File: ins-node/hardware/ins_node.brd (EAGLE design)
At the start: 54.7 x 43.2 mm, 11 parts, among them Q3 MOSFET-2N7000, U1 TINY85-20-DIP

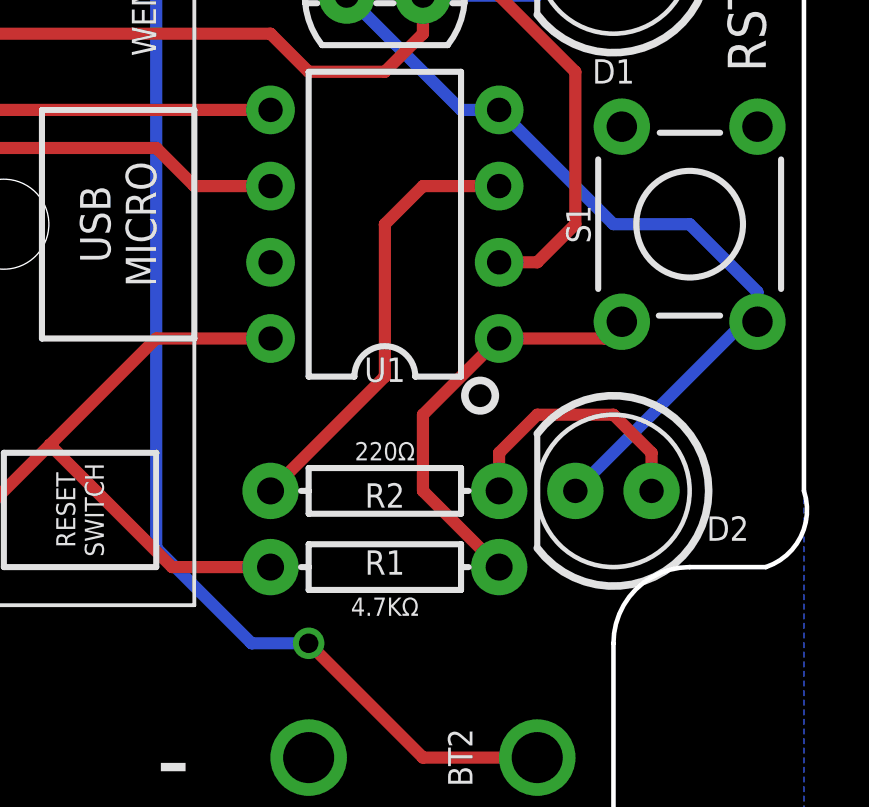
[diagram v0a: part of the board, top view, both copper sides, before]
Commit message: Add decoupling capacitor
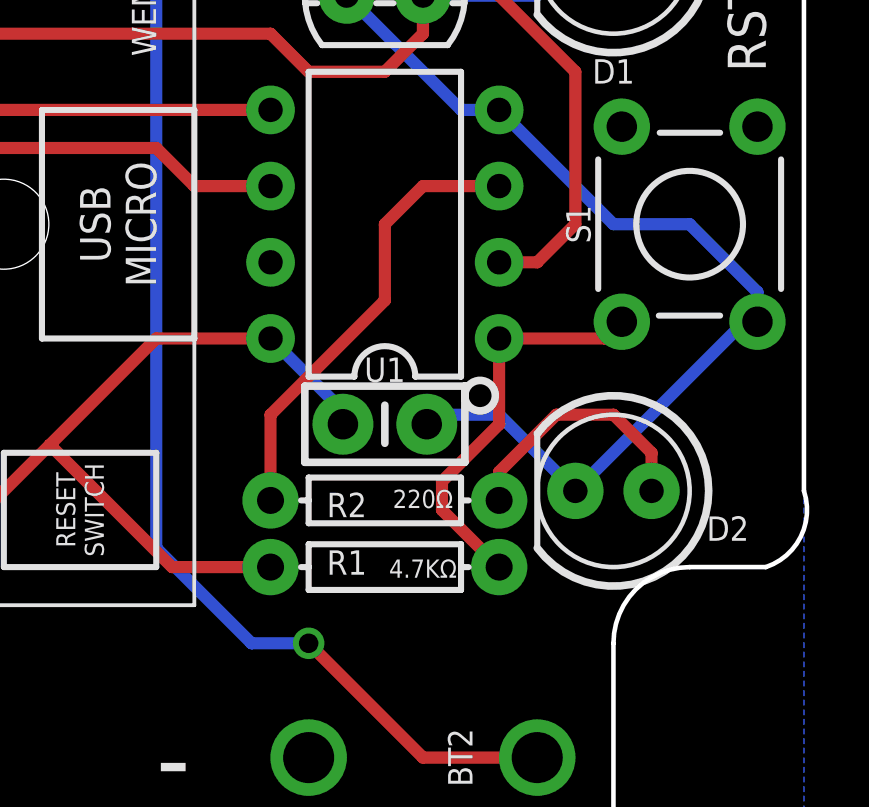
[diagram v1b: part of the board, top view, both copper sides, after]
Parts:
- added C1: 0.1uF, SparkFun-Capacitors:CAP-PTH-SMALL-KIT
- moved R2 0.32 mm to (66.0, 42.9)
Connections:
- net GND: now also C1.2
- net VCC: now also C1.1
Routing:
- net GND: track 80.6 -> 86.7 mm
- net VCC: track 52.7 -> 56.6 mm
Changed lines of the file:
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@@
 </element>
 <element name="R1" library="SparkFun-Resistors" library_urn="urn:adsk.eagle:library:532" package="AXIAL-0.3" package3d_urn="urn:adsk.eagle:package:39658/1" value="4.7KΩ" x="66.04" y="40.64" smashed="yes">
-<attribute name="NAME" x="66.04" y="40.386" size="0.8128" layer="25" font="vector" ratio="20" align="bottom-center"/>
+<attribute name="NAME" x="64.77" y="40.386" size="0.8128" layer="25" font="vector" ratio="20" align="bottom-center"/>
 <attribute name="PROD_ID" value=" " x="66.04" y="40.64" size="1.778" layer="27" display="off"/>
-<attribute name="VALUE" x="66.04" y="39.624" size="0.6096" layer="25" font="vector" ratio="20" align="top-center"/>
+<attribute name="VALUE" x="67.31" y="40.894" size="0.6096" layer="25" font="vector" ratio="20" align="top-center"/>
 </element>
-<element name="R2" library="SparkFun-Resistors" library_urn="urn:adsk.eagle:library:532" package="AXIAL-0.3" package3d_urn="urn:adsk.eagle:package:39658/1" value="220Ω" x="66.04" y="43.18" smashed="yes" rot="R180">
-<attribute name="NAME" x="66.04" y="43.434" size="0.8128" layer="25" font="vector" ratio="20" rot="R180" align="bottom-center"/>
-<attribute name="PROD_ID" value=" " x="66.04" y="43.18" size="1.778" layer="27" rot="R180" display="off"/>
-<attribute name="VALUE" x="66.04" y="44.196" size="0.6096" layer="25" font="vector" ratio="20" rot="R180" align="top-center"/>
+<element name="R2" library="SparkFun-Resistors" library_urn="urn:adsk.eagle:library:532" package="AXIAL-0.3" package3d_urn="urn:adsk.eagle:package:39658/1" value="220Ω" x="66.04" y="42.8625" smashed="yes" rot="R180">
+<attribute name="NAME" x="64.77" y="43.1165" size="0.8128" layer="25" font="vector" ratio="20" rot="R180" align="bottom-center"/>
+<attribute name="PROD_ID" value=" " x="66.04" y="42.8625" size="1.778" layer="27" rot="R180" display="off"/>
+<attribute name="VALUE" x="67.31" y="42.6085" size="0.6096" layer="25" font="vector" ratio="20" rot="R180" align="top-center"/>
 </element>
 <element name="R3" library="SparkFun-Resistors" library_urn="urn:adsk.eagle:library:532" package="AXIAL-0.3" package3d_urn="urn:adsk.eagle:package:39658/1" value="220Ω" x="66.04" y="63.5" smashed="yes" rot="R180">
@@
 <attribute name="NAME" x="77.47" y="42.3291" size="0.8128" layer="25" font="vector" ratio="20" rot="R180" align="bottom-center"/>
 <attribute name="VALUE" x="73.6346" y="46.5709" size="0.6096" layer="27" font="vector" ratio="20" rot="R180" align="top-center"/>
+</element>
+<element name="C1" library="SparkFun-Capacitors" library_urn="urn:adsk.eagle:library:510" package="CAP-PTH-SMALL-KIT" package3d_urn="urn:adsk.eagle:package:37428/1" value="0.1uF" x="66.04" y="45.4025" smashed="yes">
+<attribute name="PROD_ID" value="CAP-08370" x="66.04" y="45.4025" size="1.27" layer="27" ratio="15" display="off"/>
 </element>
 </elements>
@@
 <vertex x="25.4" y="30.48"/>
 </polygon>
+<contactref element="C1" pad="2"/>
+<wire x1="72.39" y1="43.18" x2="69.85" y2="45.72" width="0.4064" layer="16"/>
+<wire x1="69.85" y1="45.72" x2="67.7545" y2="45.72" width="0.4064" layer="16"/>
+<wire x1="67.7545" y1="45.72" x2="67.437" y2="45.4025" width="0.4064" layer="16"/>
 </signal>
 <signal name="VCC">
@@
 <wire x1="62.23" y1="40.64" x2="58.95091875" y2="40.64" width="0.4064" layer="1"/>
 <wire x1="58.95091875" y1="40.64" x2="54.875459375" y2="44.715459375" width="0.4064" layer="1"/>
+<contactref element="C1" pad="1"/>
+<wire x1="64.643" y1="45.4025" x2="64.643" y2="45.847" width="0.4064" layer="16"/>
+<wire x1="64.643" y1="45.847" x2="62.23" y2="48.26" width="0.4064" layer="16"/>
 </signal>
 <signal name="TX">
@@
 <contactref element="R2" pad="P$2"/>
 <wire x1="69.85" y1="53.34" x2="67.31" y2="53.34" width="0.4064" layer="1"/>
-<wire x1="67.31" y1="53.34" x2="66.04" y2="52.07" width="0.4064" layer="1"/>
-<wire x1="66.04" y1="52.07" x2="66.04" y2="46.99" width="0.4064" layer="1"/>
-<wire x1="66.04" y1="46.99" x2="62.23" y2="43.18" width="0.4064" layer="1"/>
+<wire x1="66.04" y1="52.07" x2="67.31" y2="53.34" width="0.4064" layer="1"/>
+<wire x1="62.23" y1="42.8625" x2="62.23" y2="45.72" width="0.4064" layer="1"/>
+<wire x1="66.04" y1="49.53" x2="66.04" y2="52.07" width="0.4064" layer="1"/>
+<wire x1="62.23" y1="45.72" x2="66.04" y2="49.53" width="0.4064" layer="1"/>
 </signal>
 <signal name="WEMOS_GND">
@@
 <contactref element="S1" pad="1"/>
 <contactref element="R1" pad="P$2"/>
-<wire x1="69.85" y1="40.64" x2="67.31" y2="43.18" width="0.4064" layer="1"/>
-<wire x1="67.31" y1="43.18" x2="67.31" y2="45.72" width="0.4064" layer="1"/>
-<wire x1="67.31" y1="45.72" x2="69.85" y2="48.26" width="0.4064" layer="1"/>
-<wire x1="69.85" y1="48.26" x2="73.3806" y2="48.26" width="0.4064" layer="1"/>
+<wire x1="70.00746875" y1="48.26" x2="73.3806" y2="48.26" width="0.4064" layer="1"/>
+<wire x1="70.00746875" y1="48.26" x2="69.85" y2="48.26" width="0.4064" layer="1"/>
 <wire x1="73.3806" y1="48.26" x2="73.9394" y2="48.8188" width="0.4064" layer="1"/>
+<wire x1="69.85" y1="40.64" x2="67.945" y2="42.545" width="0.4064" layer="1"/>
+<wire x1="67.945" y1="42.545" x2="67.945" y2="43.4975" width="0.4064" layer="1"/>
+<wire x1="67.945" y1="43.4975" x2="69.85" y2="45.4025" width="0.4064" layer="1"/>
+<wire x1="69.85" y1="45.4025" x2="69.85" y2="48.10253125" width="0.4064" layer="1"/>
+<wire x1="69.85" y1="48.10253125" x2="70.00746875" y2="48.26" width="0.4064" layer="1"/>
 </signal>
 <signal name="WEMOS_LED">
@@
 <contactref element="R2" pad="P$1"/>
 <contactref element="D2" pad="A"/>
-<wire x1="74.93" y1="43.18" x2="74.93" y2="44.45" width="0.4064" layer="1"/>
-<wire x1="74.93" y1="44.45" x2="73.66" y2="45.72" width="0.4064" layer="1"/>
-<wire x1="73.66" y1="45.72" x2="71.12" y2="45.72" width="0.4064" layer="1"/>
-<wire x1="71.12" y1="45.72" x2="69.85" y2="44.45" width="0.4064" layer="1"/>
-<wire x1="69.85" y1="44.45" x2="69.85" y2="43.18" width="0.4064" layer="1"/>
+<wire x1="69.85" y1="42.8625" x2="69.85" y2="43.815" width="0.4064" layer="1"/>
+<wire x1="71.755" y1="45.72" x2="73.66" y2="45.72" width="0.4064" layer="1"/>
+<wire x1="73.66" y1="45.72" x2="74.93" y2="44.45" width="0.4064" layer="1"/>
+<wire x1="74.93" y1="44.45" x2="74.93" y2="43.18" width="0.4064" layer="1"/>
+<wire x1="69.85" y1="43.815" x2="71.755" y2="45.72" width="0.4064" layer="1"/>
 </signal>
 </signals>

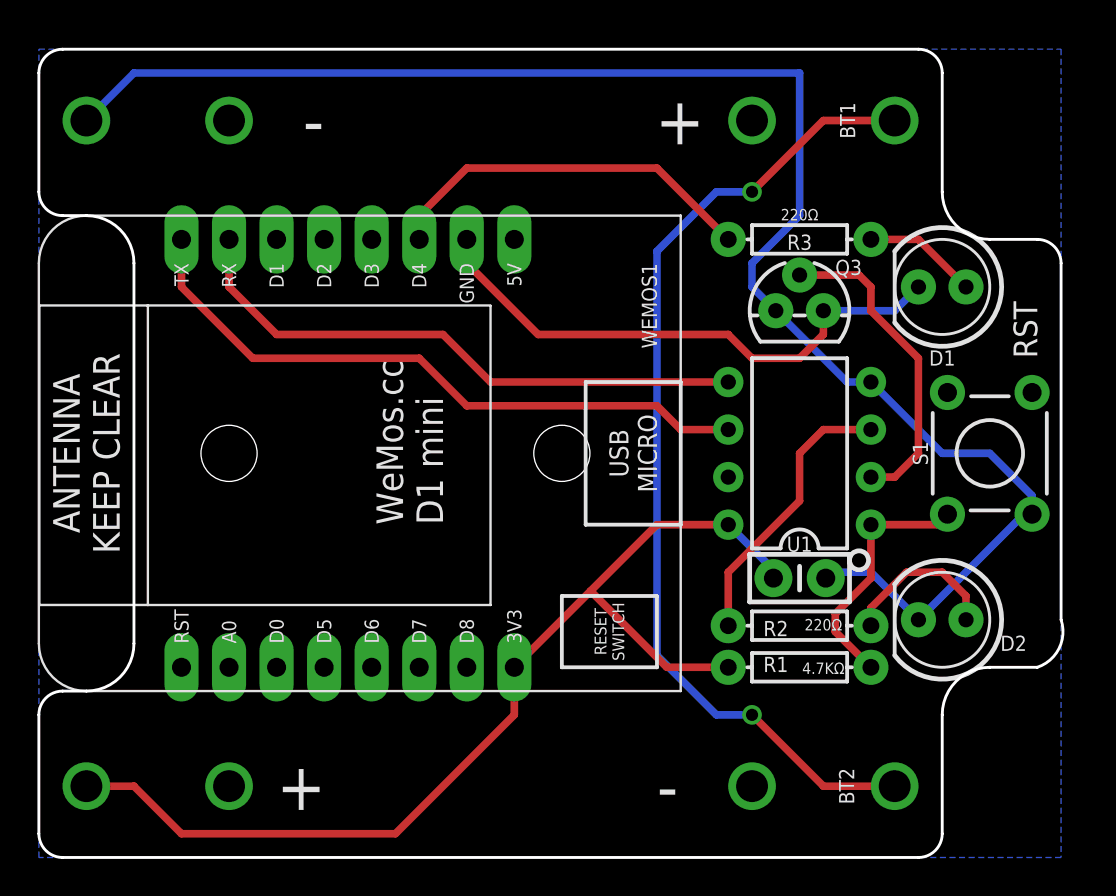
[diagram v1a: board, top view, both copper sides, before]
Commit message: Fix wifi module powering issues
HW rev.1 includes:
* 2 MOSFETs for driving the wifi module
* 3 AAA batteries
* Additional decoupling capacitor
* Board restructuring as a result of new components

Fixes #29
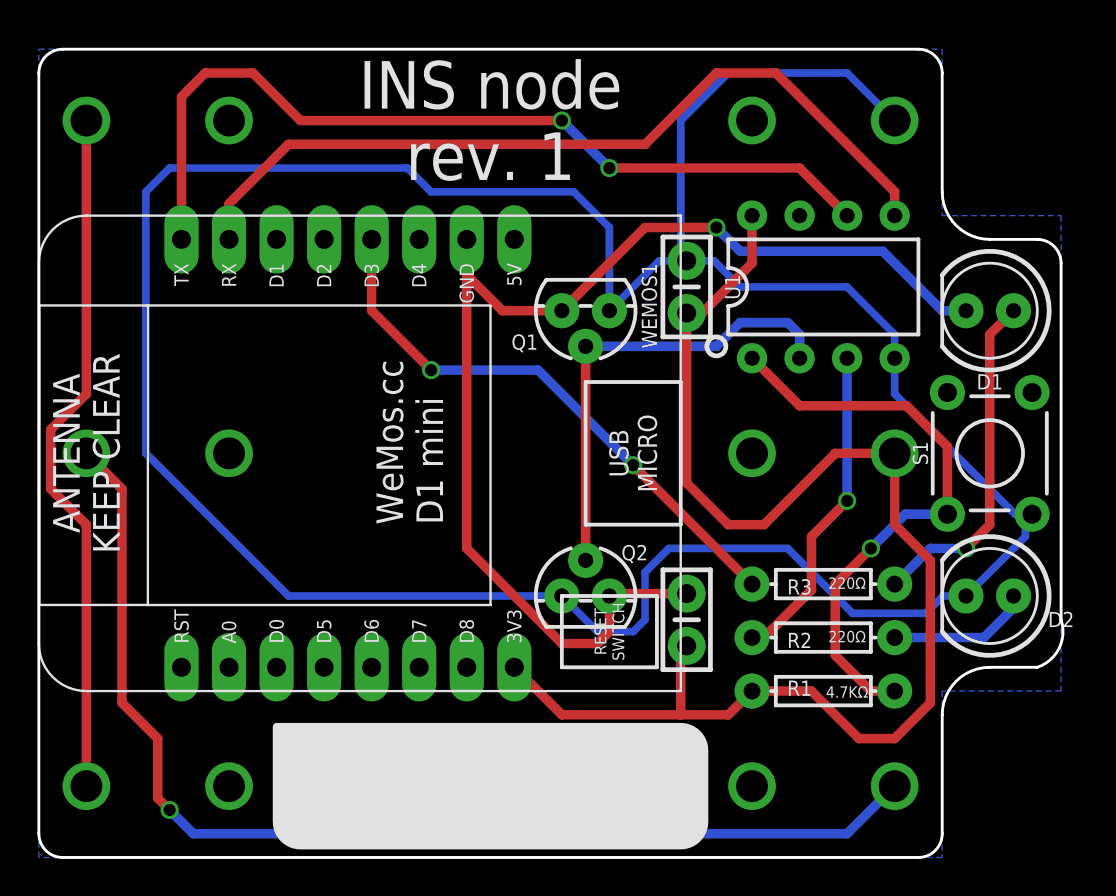
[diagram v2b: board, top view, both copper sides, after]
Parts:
- removed Q3: MOSFET-2N7000, SparkFun-DiscreteSemi:TO-92
- added BT3: (no value), SparkFun-Batteries:BATTERY-AAA
- added C2: 0.1uF, SparkFun-Capacitors:CAP-PTH-SMALL-KIT
- added Q1, Q2: MOSFET-2N7000, SparkFun-DiscreteSemi:TO-92
- moved R3 18.5 mm to (67.3, 45.1)
- moved C1 16.7 mm to (60.0, 61.0), turned to 90 degrees
- moved U1 8.98 mm to (67.3, 61.0), turned to 0 degrees
- moved D1 2.84 mm to (76.2, 59.7)
- moved D2 2.84 mm to (76.2, 44.5)
- moved R1 1.80 mm to (67.3, 39.4)
- moved R2 1.42 mm to (67.3, 42.2)
- flipped BT1 to the bottom
- flipped BT2 to the bottom
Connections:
- new net N$5: BT2.PWR@1, BT3.GND@1
- net GND: now also Q1.1, Q2.1; no longer Q3.1
- net VCC: now also BT3.PWR@1, C2.1; no longer BT2.PWR@1
- net WEMOS_GND: now also C2.2, Q1.3, Q2.3; no longer Q3.3
- net WEMOS_LED: now also WEMOS1.D3; no longer WEMOS1.D4
- net WEMOS_ON: now also Q1.2, Q2.2; no longer Q3.2
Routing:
- net GND: track 86.7 -> 157.0 mm
- net N$5: track 0.00 -> 61.2 mm, vias 0 -> 1
- net WEMOS_GND: track 29.8 -> 63.7 mm, vias 0 -> 1
- net N$2: track 13.6 -> 31.3 mm, vias 0 -> 1
- net VCC: track 56.6 -> 73.4 mm
- net N$1: track 52.8 -> 37.1 mm, vias 2 -> 0
- net TX: track 31.3 -> 44.3 mm
- net N$3: track 6.13 -> 18.4 mm, vias 0 -> 1
- net RX: track 34.9 -> 46.9 mm, vias 0 -> 2
- net WEMOS_LED: track 20.4 -> 30.2 mm, vias 0 -> 2
- net WEMOS_ON: track 17.1 -> 24.9 mm
- net ATTINY_LED: track 15.1 -> 17.4 mm, vias 0 -> 1
- net N$4: track 8.62 -> 7.64 mm
- added copper zone on layer 1, net N$6
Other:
- outline, holes or cut-outs redrawn
- board text added: "INS node rev. 1"
- board text removed: "INS node rev. 0"
- board text removed: "RST"
